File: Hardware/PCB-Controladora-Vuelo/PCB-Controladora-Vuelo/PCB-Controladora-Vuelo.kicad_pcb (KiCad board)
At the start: 2 copper layers, 40 x 90 mm, 14 parts, among them J1 Jumper Serial, J2 ESC, U1 MPU-5060, U2 ESP32-DEVKIT-V1, U3 Nrf24l01, U4 AMS1117-3.3

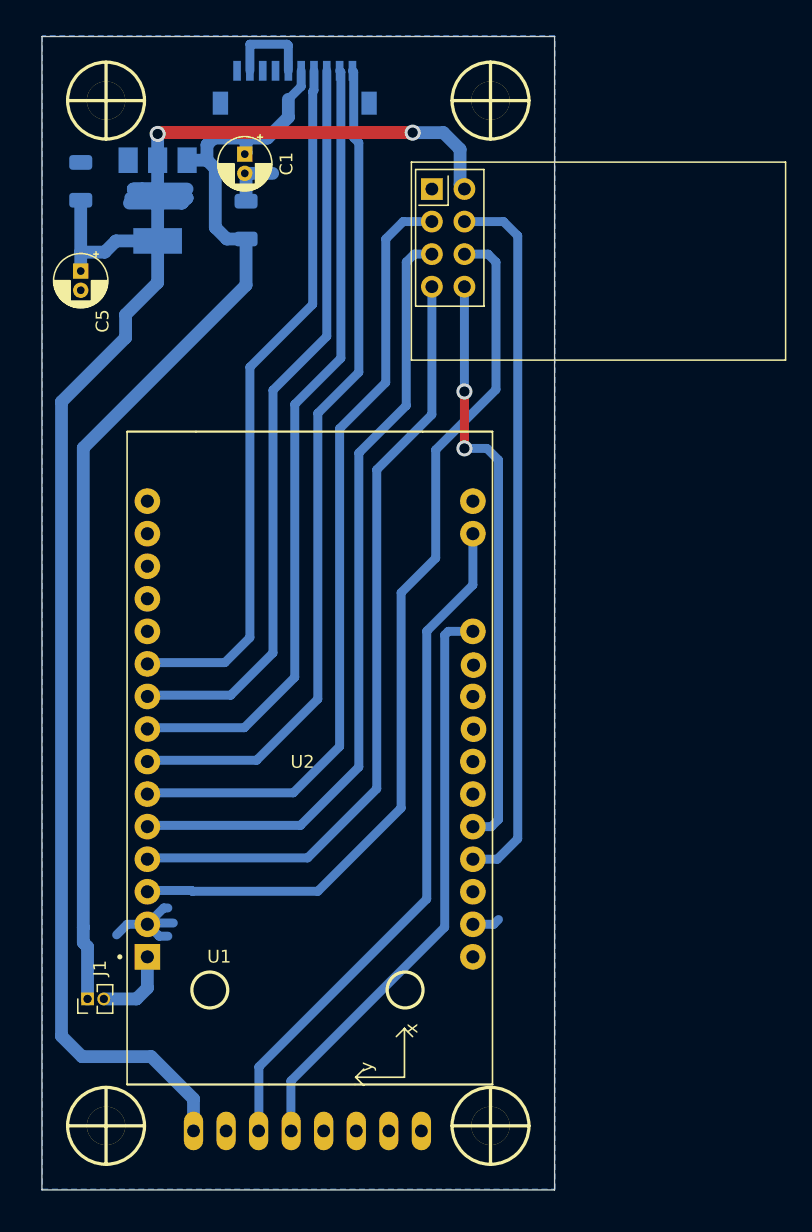
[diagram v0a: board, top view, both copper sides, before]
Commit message: Cambie pines i2c mpu6050 , hay que probarlos y cambie conexiones de nrf que funcionan, mejore las medidas para el frame
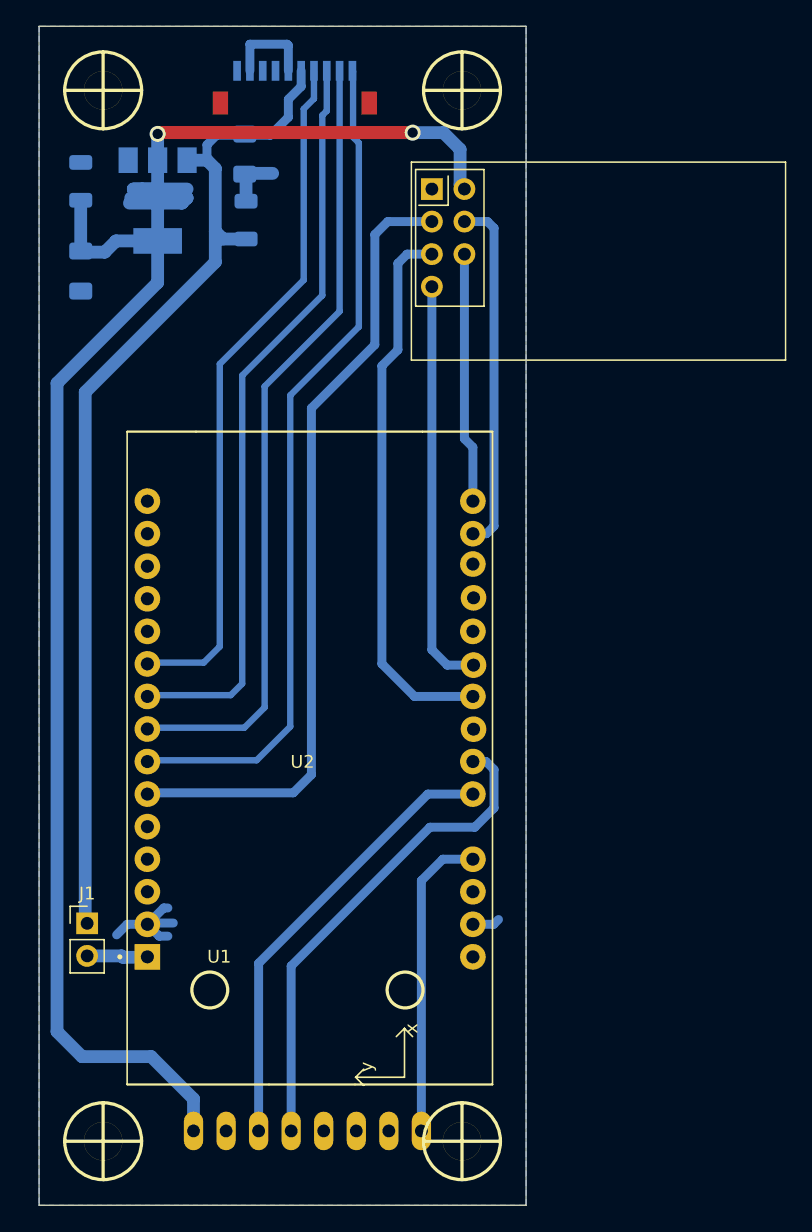
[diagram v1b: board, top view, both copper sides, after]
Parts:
- C1: value 220uF -> 10uF; footprint Capacitor_THT:CP_Radial_D4.0mm_P1.50mm -> Capacitor_SMD:C_1206_3216Metric_Pad1.33x1.80mm_HandSolder; moved to B.Cu
- C5: footprint Capacitor_THT:CP_Radial_D4.0mm_P1.50mm -> Capacitor_SMD:C_1206_3216Metric_Pad1.33x1.80mm_HandSolder; moved to B.Cu
- J1: footprint Connector_PinHeader_1.27mm:PinHeader_1x02_P1.27mm_Vertical -> Connector_PinHeader_2.54mm:PinHeader_1x02_P2.54mm_Vertical
- moved J1 5.90 mm to (117.5, 120.0), turned to 0 degrees
- moved H3 2.53 mm to (146.8, 137.0)
- moved H2 2.36 mm to (146.8, 55.0)
- moved H4 1.22 mm to (118.8, 137.0)
- moved H1 0.83 mm to (118.8, 55.0)
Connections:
- J2 pad S2: unconnected-(J2-SHIELD-PadS1) -> (no net)
- U1 pad 8: unconnected-(U1-INT-Pad8) -> /INT_MPU6050
- U2 pad 16: unconnected-(U2-D23-Pad16) -> /MOSI_NRF24L01
- U2 pad 17: /SCL_MPU6050 -> /CSN_NRF24L01
- U2 pad 20: /SDA_MPU6050 -> unconnected-(U2-D21-Pad20)
- U2 pad 21: unconnected-(U2-D19-Pad21) -> /MISO_NRF24L01
- U2 pad 22: unconnected-(U2-D18-Pad22) -> /SCK_NRF24L01
- U2 pad 24: unconnected-(U2-TX2-Pad24) -> /SDA_MPU6050
- U2 pad 25: unconnected-(U2-RX2-Pad25) -> /SCL_MPU6050
- U2 pad 27: /CSN_NRF24L01 -> /INT_MPU6050
- U2 pad 3: /MOSI_NRF24L01 -> unconnected-(U2-D13-Pad3)
- U2 pad 4: /MISO_NRF24L01 -> unconnected-(U2-D12-Pad4)
- U2 pad 5: /SCK_NRF24L01 -> unconnected-(U2-D14-Pad5)
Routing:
- net /MOSI_NRF24L01: track 70.9 -> 19.5 mm
- net /IRQ_NRF24L01: track 45.9 -> 0.00 mm, vias 2 -> 0
- net /MISO_NRF24L01: track 61.1 -> 32.1 mm
- net /CSN_NRF24L01: track 55.8 -> 27.7 mm
- net /INT_MPU6050: track 0.00 -> 24.2 mm
- net /SCK_NRF24L01: track 61.6 -> 42.9 mm
- net /SCL_MPU6050: track 53.5 -> 35.3 mm
- net +5V: track 88.3 -> 80.8 mm
- net /SDA_MPU6050: track 46.0 -> 38.7 mm
- net /Jumper_Serial: track 6.32 -> 4.89 mm
- net +3V3: track 143.0 -> 141.8 mm
- net /S1_MOTOR: track 55.1 -> 54.2 mm
- net /CE_NRF24L01: track 61.8 -> 62.5 mm
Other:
- board size 40 x 90 mm -> 38 x 92 mm

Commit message: cambie pines sda y scl para evitar conflictos wifi
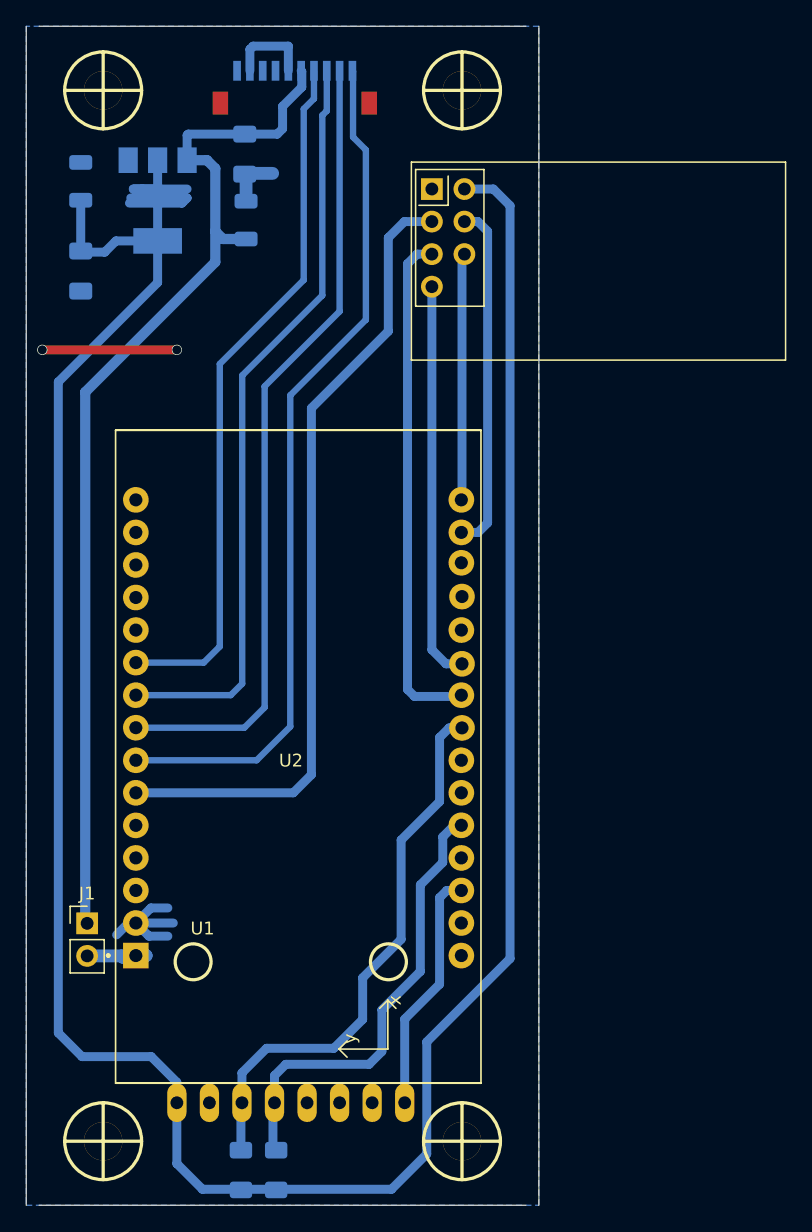
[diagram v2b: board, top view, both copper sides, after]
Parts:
- added R1: 4,7k, Resistor_SMD:R_1206_3216Metric_Pad1.30x1.75mm_HandSolder, B.Cu at (132.2, 139.2)
- added R2: 4,7k, Resistor_SMD:R_1206_3216Metric_Pad1.30x1.75mm_HandSolder, B.Cu at (129.5, 139.2)
- moved U1 2.56 mm to (124.5, 134.0)
- moved U2 0.91 mm to (133.5, 107.0)
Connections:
- J2 pad S2: (no net) -> unconnected-(J2-SHIELD-PadS1)
- U2 pad 18: (no net) -> unconnected-(U2-TXD-Pad18)
- U2 pad 19: (no net) -> unconnected-(U2-RXD-Pad19)
- U2 pad 23: unconnected-(U2-D5-Pad23) -> /SCL_MPU6050
- U2 pad 24: /SDA_MPU6050 -> unconnected-(U2-TX2-Pad24)
- U2 pad 25: /SCL_MPU6050 -> unconnected-(U2-RX2-Pad25)
- U2 pad 27: /INT_MPU6050 -> unconnected-(U2-D2-Pad27)
- U2 pad 28: unconnected-(U2-D2-Pad28) -> /INT_MPU6050
- U2 pad 29: GND -> (no net)
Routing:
- net +3V3: track 141.8 -> 216.3 mm, vias 2 -> 0
- net GND: track 22.6 -> 32.3 mm, vias 0 -> 2
- net /SCL_MPU6050: track 35.3 -> 43.3 mm
- net /INT_MPU6050: track 24.2 -> 19.1 mm
- net /SDA_MPU6050: track 38.7 -> 35.1 mm
- net /SCK_NRF24L01: track 42.9 -> 39.9 mm
- net +5V: track 80.8 -> 83.1 mm
- net /S4_MOTOR: track 65.9 -> 67.2 mm
- net /MISO_NRF24L01: track 32.1 -> 31.1 mm
- net /S1_MOTOR: track 54.2 -> 55.0 mm
- net /S3_MOTOR: track 61.9 -> 62.8 mm
- net /S2_MOTOR: track 58.4 -> 59.2 mm
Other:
- board size 38 x 92 mm -> 40 x 92 mm

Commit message: placa realizada en taller , prueba de pines
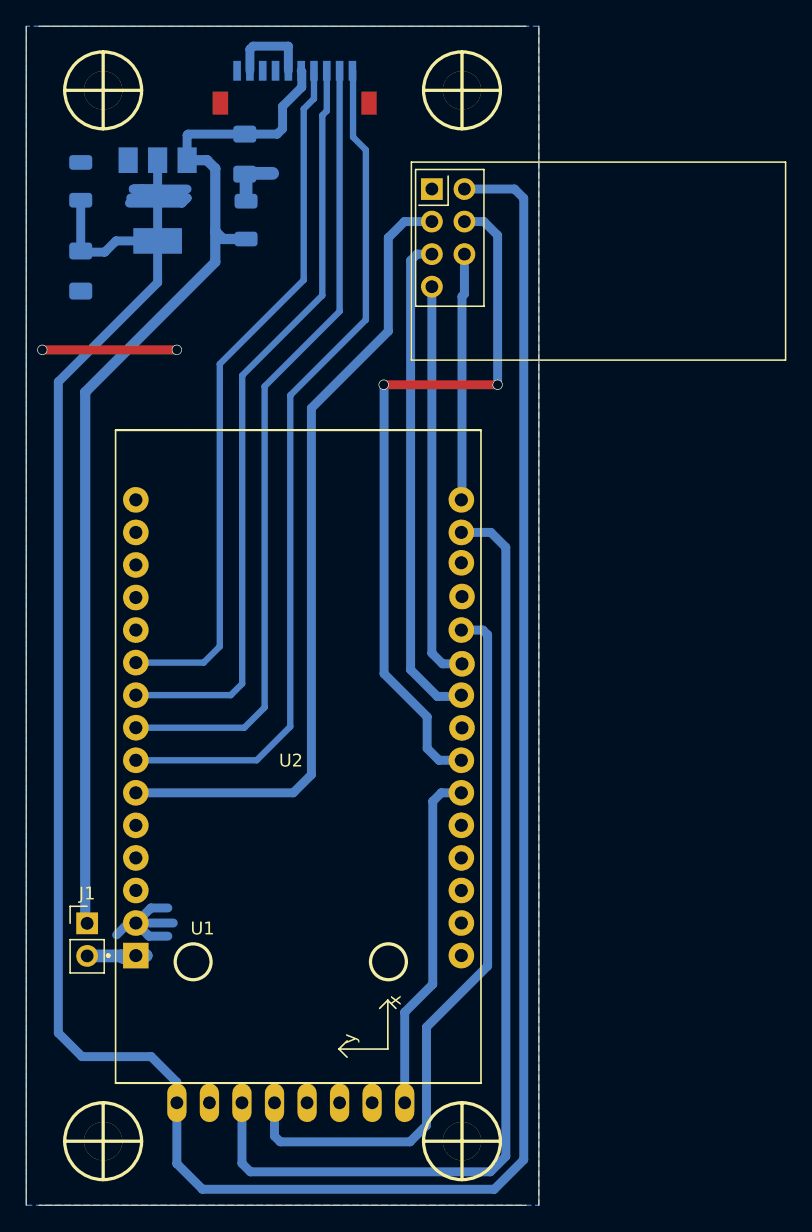
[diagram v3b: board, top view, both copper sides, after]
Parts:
- removed R1, R2: 4,7k, Resistor_SMD:R_1206_3216Metric_Pad1.30x1.75mm_HandSolder
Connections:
- U2 pad 17: /CSN_NRF24L01 -> /SCL_MPU6050
- U2 pad 20: unconnected-(U2-D21-Pad20) -> /SDA_MPU6050
- U2 pad 23: /SCL_MPU6050 -> unconnected-(U2-D5-Pad23)
- U2 pad 24: unconnected-(U2-TX2-Pad24) -> /CSN_NRF24L01
- U2 pad 25: unconnected-(U2-RX2-Pad25) -> /INT_MPU6050
- U2 pad 26: /SDA_MPU6050 -> unconnected-(U2-D4-Pad26)
- U2 pad 28: /INT_MPU6050 -> unconnected-(U2-D15-Pad28)
- U2 pad 29: (no net) -> GND
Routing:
- net /SCL_MPU6050: track 43.3 -> 77.7 mm
- net /CSN_NRF24L01: track 27.2 -> 56.4 mm, vias 0 -> 2
- net /SDA_MPU6050: track 35.1 -> 57.8 mm
- net /INT_MPU6050: track 19.1 -> 26.9 mm
- net +3V3: track 216.3 -> 222.9 mm
- net /SCK_NRF24L01: track 39.9 -> 38.7 mm
